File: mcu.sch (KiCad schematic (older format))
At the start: 1 part, among them U3 STM32F407VETx

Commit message: Hook up peripherals
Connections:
- net I2Sext_SD: now reaches U3.17 (PC2)
- net I2S_SD: now reaches U3.18 (PC3)
- net ~RESET: now reaches U3.35 (PB0)
- net BCLK: now reaches U3.47 (PB10)
- net MCLK: now reaches U3.66 (PC9)
- net SCL: now reaches U3.92 (PB6)
- net SDA: now reaches U3.93 (PB7)
- net WCLK: now reaches U3.96 (PB9)
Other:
- note added: "MCO2"
- note added: "data in"
- note added: "data out"
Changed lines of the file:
@@
 	1    0    0    -1
 $EndComp
+Text HLabel 4100 5700 2    50   Output ~ 0
+MCLK
+Text HLabel 4150 4100 2    50   Input ~ 0
+BCLK
+Text HLabel 4150 4000 2    50   Input ~ 0
+WCLK
+Text HLabel 4150 3100 2    50   Output ~ 0
+~RESET
+Text HLabel 4150 3700 2    50   Output ~ 0
+SCL
+Text HLabel 4150 3800 2    50   BiDi ~ 0
+SDA
+Text HLabel 4100 5100 2    50   Output ~ 0
+I2S_SD
+Text HLabel 4100 5000 2    50   Input ~ 0
+I2Sext_SD
+Wire Wire Line
+	4100 5100 3900 5100
+Wire Wire Line
+	4100 5000 3900 5000
+Wire Wire Line
+	4100 5700 3900 5700
+Text Notes 4400 5700 0    50   ~ 0
+MCO2
+Text Notes 4550 5000 0    50   ~ 0
+data in
+Text Notes 4550 5100 0    50   ~ 0
+data out
+Wire Wire Line
+	4150 4000 3900 4000
+Wire Wire Line
+	4150 4100 3900 4100
+Wire Wire Line
+	4150 3100 3900 3100
+Wire Wire Line
+	4150 3700 3900 3700
+Wire Wire Line
+	4150 3800 3900 3800
 $EndSCHEMATC

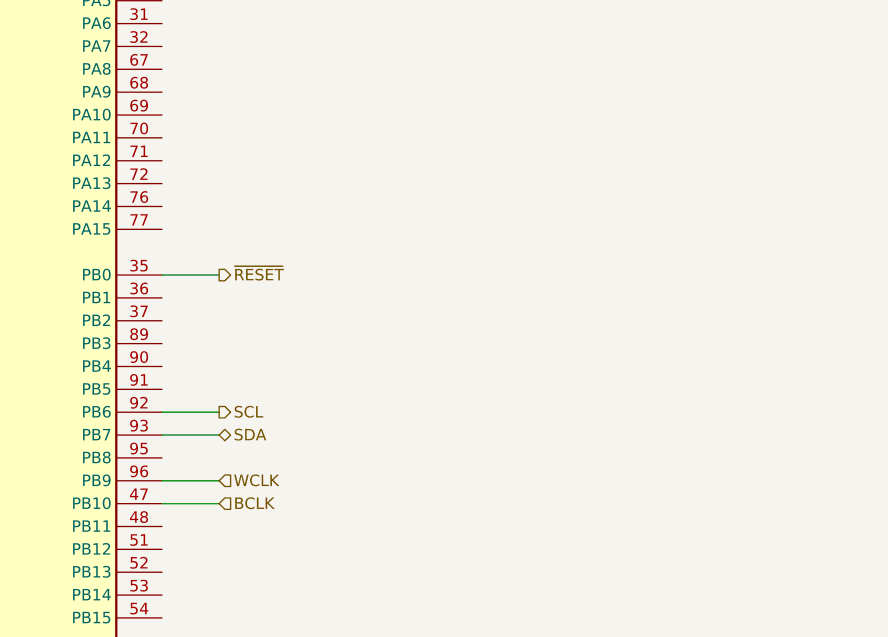
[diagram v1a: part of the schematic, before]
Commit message: Add debug header
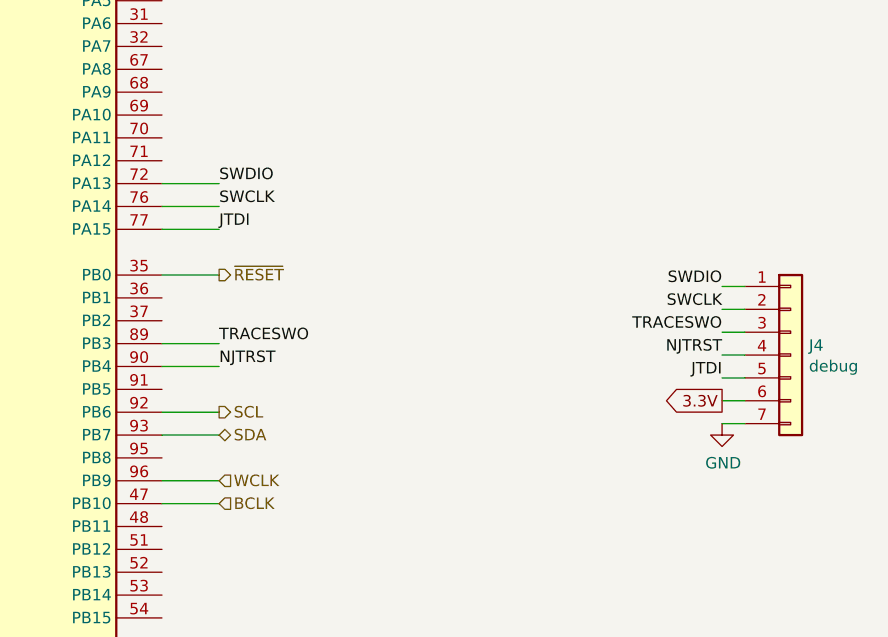
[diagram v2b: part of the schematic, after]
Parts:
- added J4: debug, symbol Connector_Generic:Conn_01x07
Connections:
- net SWDIO: now reaches U3.72 (PA13)
- net SWDIO: now also J4.1 (Pin_1)
- net SWCLK: now reaches U3.76 (PA14)
- net SWCLK: now also J4.2 (Pin_2)
- net JTDI: now reaches U3.77 (PA15)
- net JTDI: now also J4.5 (Pin_5)
- net TRACESWO: now reaches U3.89 (PB3)
- net TRACESWO: now also J4.3 (Pin_3)
- net NJTRST: now reaches U3.90 (PB4)
- net NJTRST: now also J4.4 (Pin_4)
- new net 3.3V: J4.6 (Pin_6)
- new net GND: J4.7 (Pin_7)
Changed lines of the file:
@@
 Wire Wire Line
 	4150 3800 3900 3800
+Text Label 6350 3150 2    50   ~ 0
+SWDIO
+Wire Wire Line
+	6350 3150 6450 3150
+Text Label 6350 3250 2    50   ~ 0
+SWCLK
+Text Label 6350 3550 2    50   ~ 0
+JTDI
+Text Label 6350 3350 2    50   ~ 0
+TRACESWO
+Wire Wire Line
+	6350 3250 6450 3250
+Wire Wire Line
+	6350 3650 6450 3650
+Text Label 6350 3450 2    50   ~ 0
+NJTRST
+Wire Wire Line
+	6350 3450 6450 3450
+Wire Wire Line
+	6350 3350 6450 3350
+Wire Wire Line
+	6350 3550 6450 3550
+Text GLabel 6350 3650 0    50   Output ~ 0
+3.3V
+$Comp
+L power:GND #PWR010
+U 1 1 60166405
+P 6350 3750
+F 0 "#PWR010" H 6350 3500 50  0001 C CNN
+F 1 "GND" H 6355 3577 50  0000 C CNN
+F 2 "" H 6350 3750 50  0001 C CNN
+F 3 "" H 6350 3750 50  0001 C CNN
+	1    6350 3750
+	1    0    0    -1
+$EndComp
+Wire Wire Line
+	6350 3750 6450 3750
+$Comp
+L Connector_Generic:Conn_01x07 J4
+U 1 1 601675AC
+P 6650 3450
+F 0 "J4" H 6730 3492 50  0000 L CNN
+F 1 "debug" H 6730 3401 50  0000 L CNN
+F 2 "" H 6650 3450 50  0001 C CNN
+F 3 "~" H 6650 3450 50  0001 C CNN
+	1    6650 3450
+	1    0    0    -1
+$EndComp
+Text Label 4150 2700 0    50   ~ 0
+SWDIO
+Wire Wire Line
+	4150 2700 3900 2700
+Text Label 4150 2800 0    50   ~ 0
+SWCLK
+Wire Wire Line
+	4150 2800 3900 2800
+Text Label 4150 2900 0    50   ~ 0
+JTDI
+Wire Wire Line
+	4150 2900 3900 2900
+Text Label 4150 3400 0    50   ~ 0
+TRACESWO
+Wire Wire Line
+	4150 3400 3900 3400
+Text Label 4150 3500 0    50   ~ 0
+NJTRST
+Wire Wire Line
+	4150 3500 3900 3500
 $EndSCHEMATC

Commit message: Use a better codec
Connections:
- net SCLK: now reaches U3.78 (PC10)
- net ~CSB: now reaches U3.79 (PC11)
- net SDOUT: now reaches U3.80 (PC12)
- net SCL: no longer names the net of U3.92 (PB6)
- net SDA: no longer names the net of U3.93 (PB7)
- net ~RESET: no longer names the net of U3.35 (PB0)
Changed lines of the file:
@@
 Text HLabel 4150 4000 2    50   Input ~ 0
 WCLK
-Text HLabel 4150 3100 2    50   Output ~ 0
-~RESET
-Text HLabel 4150 3700 2    50   Output ~ 0
-SCL
-Text HLabel 4150 3800 2    50   BiDi ~ 0
-SDA
 Text HLabel 4100 5100 2    50   Output ~ 0
 I2S_SD
@@
 Wire Wire Line
 	4150 4100 3900 4100
-Wire Wire Line
-	4150 3100 3900 3100
-Wire Wire Line
-	4150 3700 3900 3700
-Wire Wire Line
-	4150 3800 3900 3800
 Text Label 6350 3150 2    50   ~ 0
 SWDIO
@@
 Wire Wire Line
 	4150 3500 3900 3500
+Text HLabel 4100 5800 2    50   Output ~ 0
+SCLK
+Text HLabel 4100 5900 2    50   Output ~ 0
+~CSB
+Text HLabel 4100 6000 2    50   Output ~ 0
+SDOUT
+Wire Wire Line
+	4100 6000 3900 6000
+Wire Wire Line
+	4100 5800 3900 5800
+Wire Wire Line
+	4100 5900 3900 5900
 $EndSCHEMATC

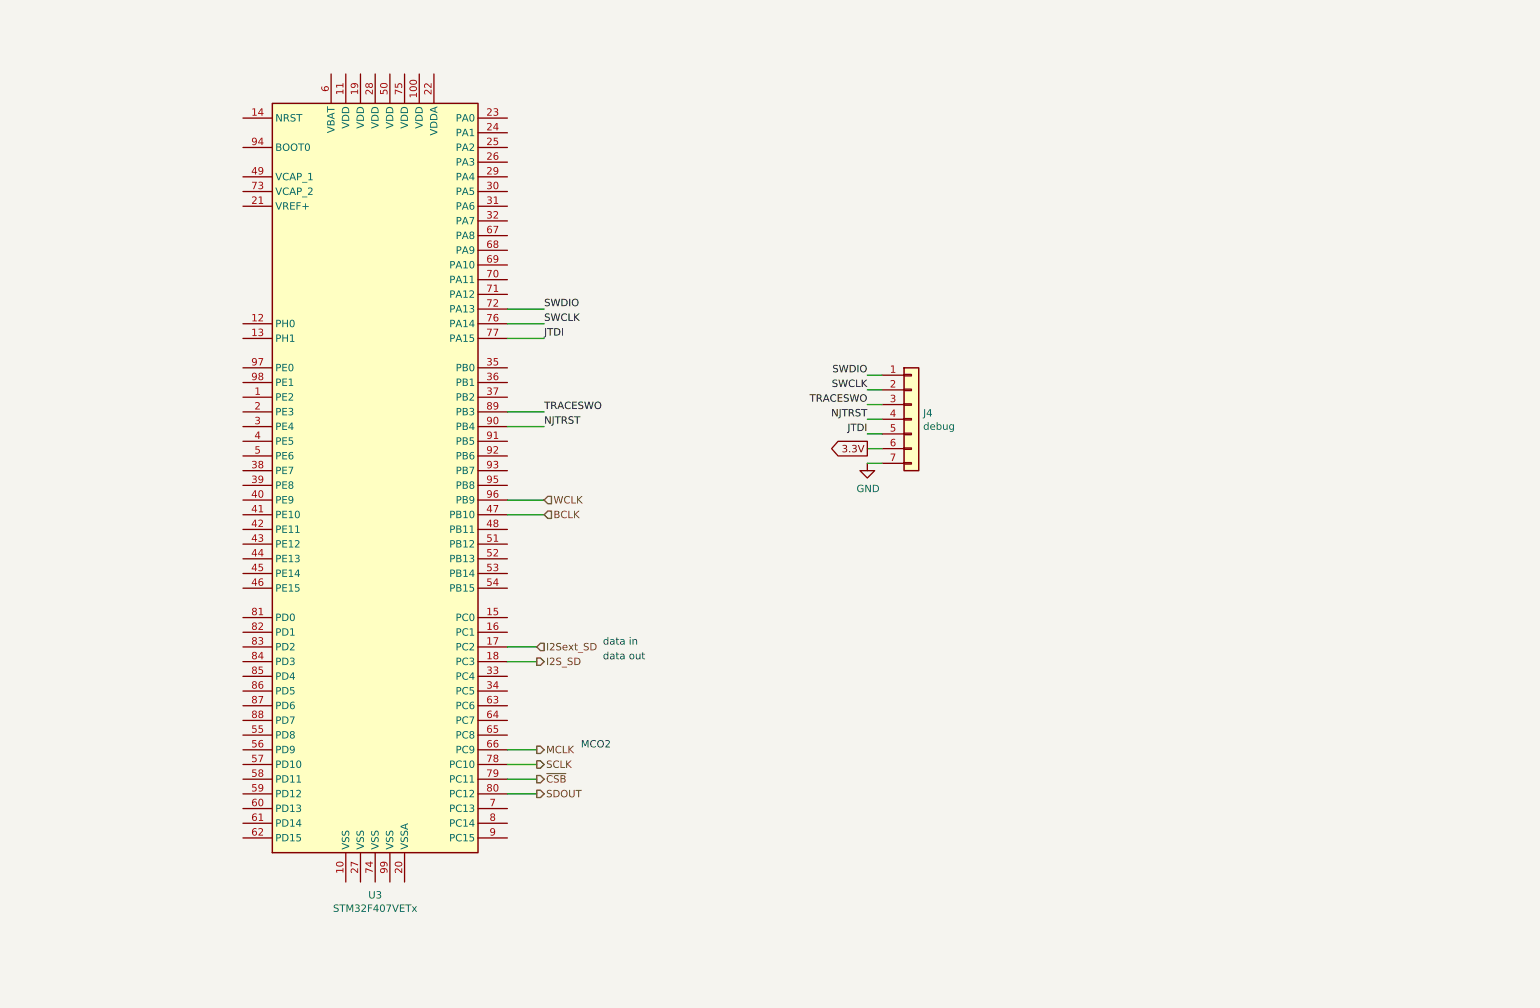
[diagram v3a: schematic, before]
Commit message: Power the MCU
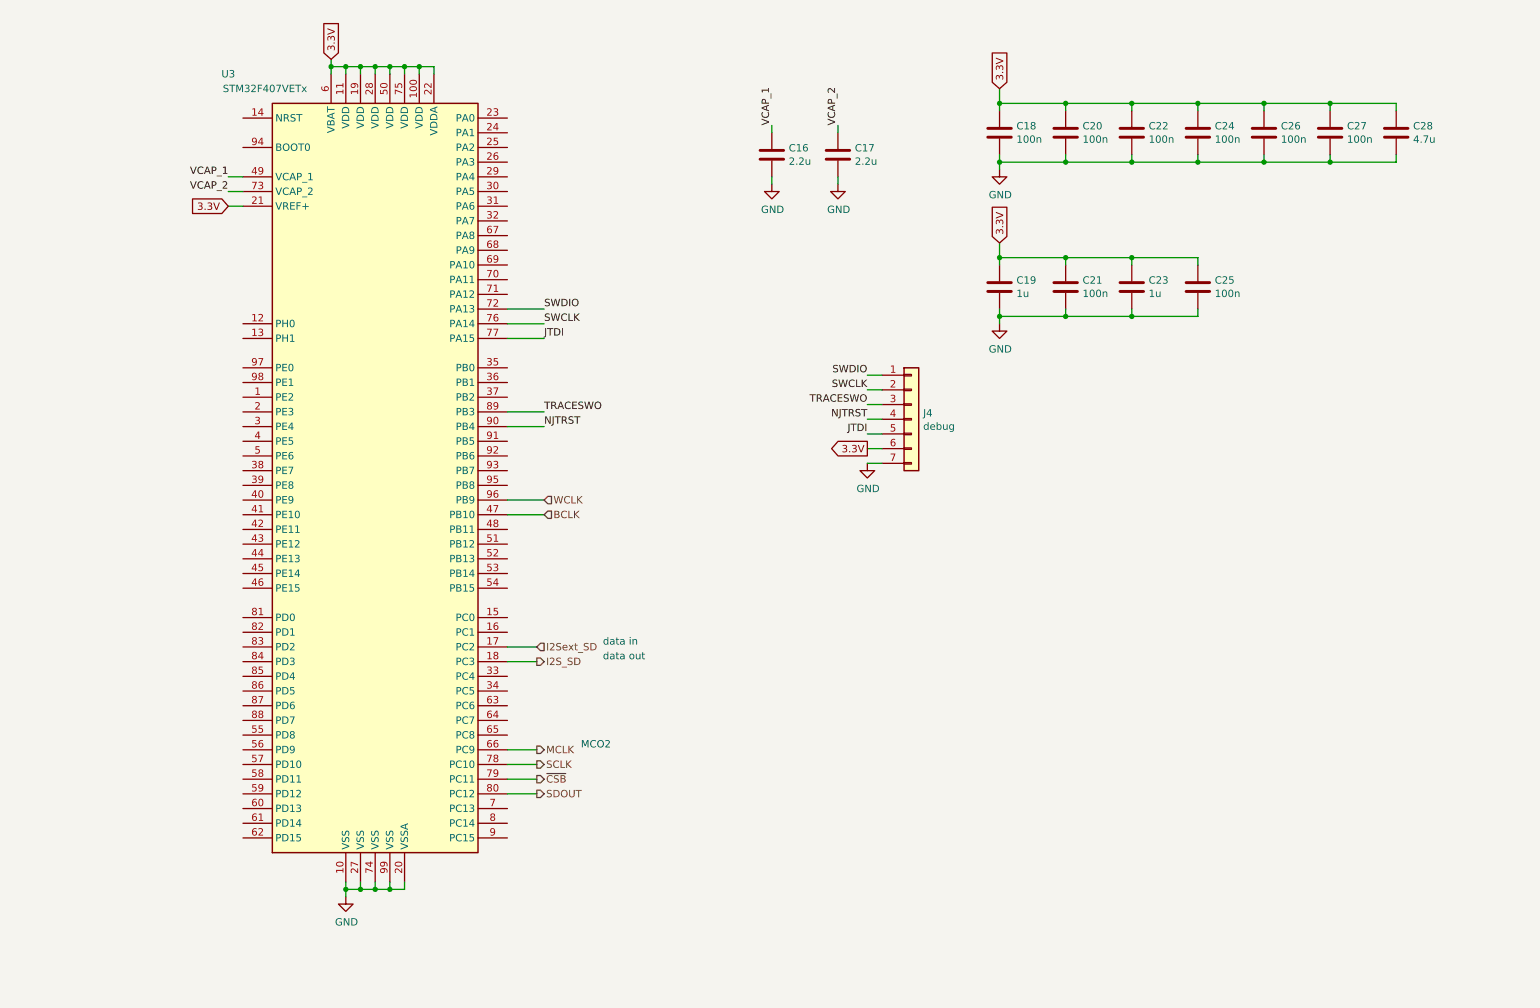
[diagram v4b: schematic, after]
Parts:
- added C16, C17: 2.2u, symbol Device:C
- added C18, C20, C21, C22, C24, C25, C26, C27: 100n, symbol Device:C
- added C19, C23: 1u, symbol Device:C
- added C28: 4.7u, symbol Device:C
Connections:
- net 3.3V: now also U3.100 (VDD), U3.11 (VDD), U3.19 (VDD), U3.21 (VREF+), U3.22 (VDDA), U3.28 (VDD), U3.50 (VDD), U3.6 (VBAT), U3.75 (VDD), C18.1, C19.1, C20.1, C21.1, C22.1, C23.1, C24.1, C25.1, C26.1, C27.1, C28.1
- net GND: now also U3.10 (VSS), U3.20 (VSSA), U3.27 (VSS), U3.74 (VSS), U3.99 (VSS), C16.2, C17.2, C18.2, C19.2, C20.2, C21.2, C22.2, C23.2, C24.2, C25.2, C26.2, C27.2, C28.2
- net VCAP_1: now reaches U3.49 (VCAP_1)
- net VCAP_1: now also C16.1
- net VCAP_2: now reaches U3.73 (VCAP_2)
- net VCAP_2: now also C17.1

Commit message: Coupling caps, crystals
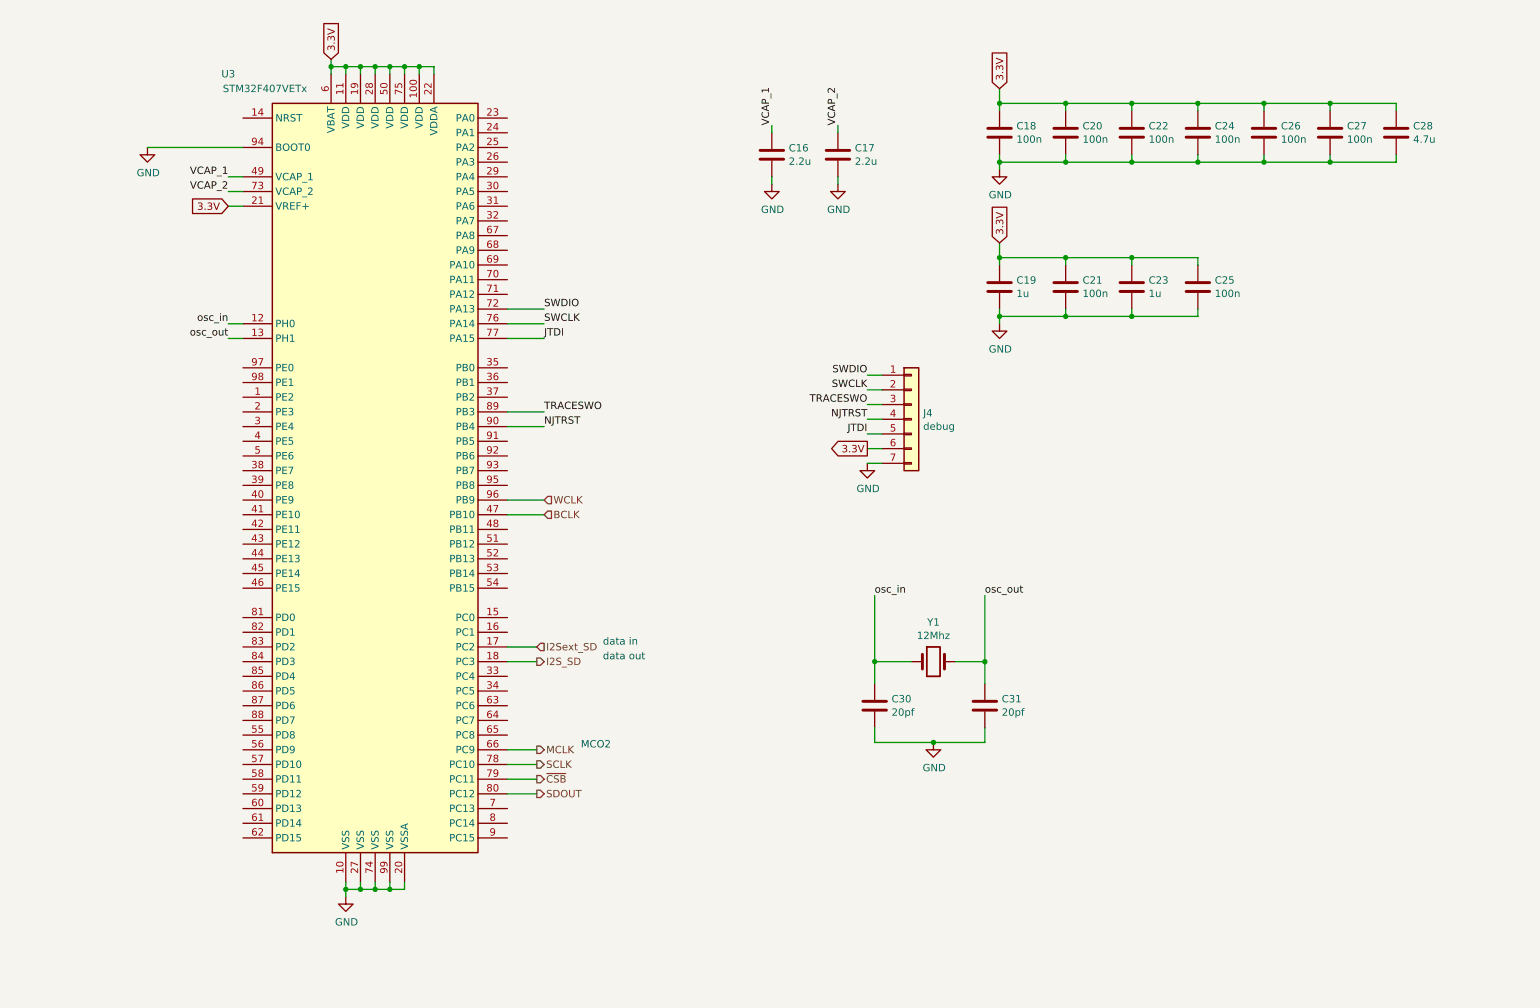
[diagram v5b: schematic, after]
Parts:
- added C30, C31: 20pf, symbol Device:C
- added Y1: 12Mhz, symbol Device:Crystal
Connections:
- net GND: now also U3.94 (BOOT0), C30.2, C31.2
- net osc_in: now reaches U3.12 (PH0)
- net osc_in: now also C30.1, Y1.1
- net osc_out: now reaches U3.13 (PH1)
- net osc_out: now also C31.1, Y1.2
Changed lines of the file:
@@
 Connection ~ 2700 1050
 Connection ~ 2800 1050
+$Comp
+L power:GND #PWR018
+U 1 1 6007ECDF
+P 1450 1600
+F 0 "#PWR018" H 1450 1350 50  0001 C CNN
+F 1 "GND" H 1455 1427 50  0000 C CNN
+F 2 "" H 1450 1600 50  0001 C CNN
+F 3 "" H 1450 1600 50  0001 C CNN
+	1    1450 1600
+	1    0    0    -1
+$EndComp
+Wire Wire Line
+	1450 1600 2100 1600
+$Comp
+L Device:Crystal Y1
+U 1 1 600E34F2
+P 6800 5100
+F 0 "Y1" H 6800 5368 50  0000 C CNN
+F 1 "12Mhz" H 6800 5277 50  0000 C CNN
+F 2 "" H 6800 5100 50  0001 C CNN
+F 3 "~" H 6800 5100 50  0001 C CNN
+	1    6800 5100
+	1    0    0    -1
+$EndComp
+Text Label 2000 2800 2    50   ~ 0
+osc_in
+Wire Wire Line
+	2000 2800 2100 2800
+Wire Wire Line
+	2000 2900 2100 2900
+Text Label 2000 2900 2    50   ~ 0
+osc_out
+$Comp
+L Device:C C30
+U 1 1 600EA749
+P 6400 5400
+F 0 "C30" H 6515 5446 50  0000 L CNN
+F 1 "20pf" H 6515 5355 50  0000 L CNN
+F 2 "" H 6438 5250 50  0001 C CNN
+F 3 "~" H 6400 5400 50  0001 C CNN
+	1    6400 5400
+	1    0    0    -1
+$EndComp
+$Comp
+L Device:C C31
+U 1 1 600EB2AF
+P 7150 5400
+F 0 "C31" H 7265 5446 50  0000 L CNN
+F 1 "20pf" H 7265 5355 50  0000 L CNN
+F 2 "" H 7188 5250 50  0001 C CNN
+F 3 "~" H 7150 5400 50  0001 C CNN
+	1    7150 5400
+	1    0    0    -1
+$EndComp
+Wire Wire Line
+	7150 5250 7150 5100
+Wire Wire Line
+	7150 5100 6950 5100
+Wire Wire Line
+	6400 5250 6400 5100
+Wire Wire Line
+	6400 5100 6650 5100
+Wire Wire Line
+	6400 5550 6400 5650
+Wire Wire Line
+	6400 5650 6800 5650
+Wire Wire Line
+	7150 5650 7150 5550
+$Comp
+L power:GND #PWR019
+U 1 1 600F5882
+P 6800 5650
+F 0 "#PWR019" H 6800 5400 50  0001 C CNN
+F 1 "GND" H 6805 5477 50  0000 C CNN
+F 2 "" H 6800 5650 50  0001 C CNN
+F 3 "" H 6800 5650 50  0001 C CNN
+	1    6800 5650
+	1    0    0    -1
+$EndComp
+Connection ~ 6800 5650
+Wire Wire Line
+	6800 5650 7150 5650
+Wire Wire Line
+	6400 5100 6400 4650
+Connection ~ 6400 5100
+Wire Wire Line
+	7150 5100 7150 4650
+Connection ~ 7150 5100
+Text Label 7150 4650 0    50   ~ 0
+osc_out
+Text Label 6400 4650 0    50   ~ 0
+osc_in
 $EndSCHEMATC

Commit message: Clean things up, add LEDs, aux stuff
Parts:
- added D1, D2, D3, D4: LED, symbol Device:LED
- added J5, J6: Conn_01x16_Male, symbol Connector:Conn_01x16_Male
- added R10, R7, R8, R9: 75, symbol Device:R
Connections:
- net GND: now also D1.1 (K), D2.1 (K), D3.1 (K), D4.1 (K)
- net at U3.1 (PE2): now also J5.3 (Pin_3)
- net at U3.2 (PE3): now also J5.4 (Pin_4)
- net led1: now reaches U3.23 (PA0)
- net led1: now also R7.2
- net led2: now reaches U3.24 (PA1)
- net led2: now also R8.2
- net led3: now reaches U3.25 (PA2)
- net led3: now also R9.2
- net led4: now reaches U3.26 (PA3)
- net led4: now also R10.2
- net at U3.3 (PE4): now also J5.5 (Pin_5)
- net at U3.38 (PE7): now also J5.8 (Pin_8)
- net at U3.39 (PE8): now also J5.9 (Pin_9)
- net at U3.4 (PE5): now also J5.6 (Pin_6)
- net at U3.40 (PE9): now also J5.10 (Pin_10)
- net at U3.41 (PE10): now also J5.11 (Pin_11)
- net at U3.42 (PE11): now also J5.12 (Pin_12)
- net at U3.43 (PE12): now also J5.13 (Pin_13)
- net at U3.44 (PE13): now also J5.14 (Pin_14)
- net at U3.45 (PE14): now also J5.15 (Pin_15)
- net at U3.46 (PE15): now also J5.16 (Pin_16)
- net at U3.5 (PE6): now also J5.7 (Pin_7)
- net at U3.55 (PD8): now also J6.9 (Pin_9)
- net at U3.56 (PD9): now also J6.10 (Pin_10)
- net at U3.57 (PD10): now also J6.11 (Pin_11)
- net at U3.58 (PD11): now also J6.12 (Pin_12)
- net at U3.59 (PD12): now also J6.13 (Pin_13)
- net at U3.60 (PD13): now also J6.14 (Pin_14)
- net at U3.61 (PD14): now also J6.15 (Pin_15)
- net at U3.62 (PD15): now also J6.16 (Pin_16)
- net at U3.81 (PD0): now also J6.1 (Pin_1)
- net at U3.82 (PD1): now also J6.2 (Pin_2)
- net at U3.83 (PD2): now also J6.3 (Pin_3)
- net at U3.84 (PD3): now also J6.4 (Pin_4)
- net at U3.85 (PD4): now also J6.5 (Pin_5)
- net at U3.86 (PD5): now also J6.6 (Pin_6)
- net at U3.87 (PD6): now also J6.7 (Pin_7)
- net at U3.88 (PD7): now also J6.8 (Pin_8)
- net at U3.97 (PE0): now also J5.1 (Pin_1)
- net at U3.98 (PE1): now also J5.2 (Pin_2)
- new net: D1.2 (A), R7.1
- new net: D2.2 (A), R8.1
- new net: D3.2 (A), R9.1
- new net: D4.2 (A), R10.1

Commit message: USB
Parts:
- added J10: USB_C_Receptacle_USB2.0, symbol Connector:USB_C_Receptacle_USB2.0
- added R? (x2): 5.1k, symbol Device:R
- added R?: 1M, symbol Device:R
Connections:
- net GND: now also J10.A1 (GND), J10.A12 (GND), J10.B1 (GND), J10.B12 (GND), J10.S1 (SHIELD), R?.2, R?.2, R?.2
- net VBUS: now reaches U3.68 (PA9)
- net VBUS: now also J10.A4 (VBUS), J10.A9 (VBUS), J10.B4 (VBUS), J10.B9 (VBUS), R?.1
- net OTG_FS_DM: now reaches U3.70 (PA11)
- net OTG_FS_DM: now also J10.A7 (D-), J10.B7 (D-)
- net OTG_FS_DP: now reaches U3.71 (PA12)
- net OTG_FS_DP: now also J10.A6 (D+), J10.B6 (D+)
- new net: J10.A5 (CC1), R?.1
- new net: J10.B5 (CC2), R?.1
- no-connect marks 0 -> 2
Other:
- moved on the sheet: C30, C31, D1, D2, D3, D4, J4, R10, R7, R8, R9, Y1
